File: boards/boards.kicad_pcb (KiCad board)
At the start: 2 copper layers, 34 parts, among them J1 MicroSD, P1 CONN_01X04, P10 , P11 , P12 , P13 CONN_01X02, P2 , P3 , P4 , P5 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

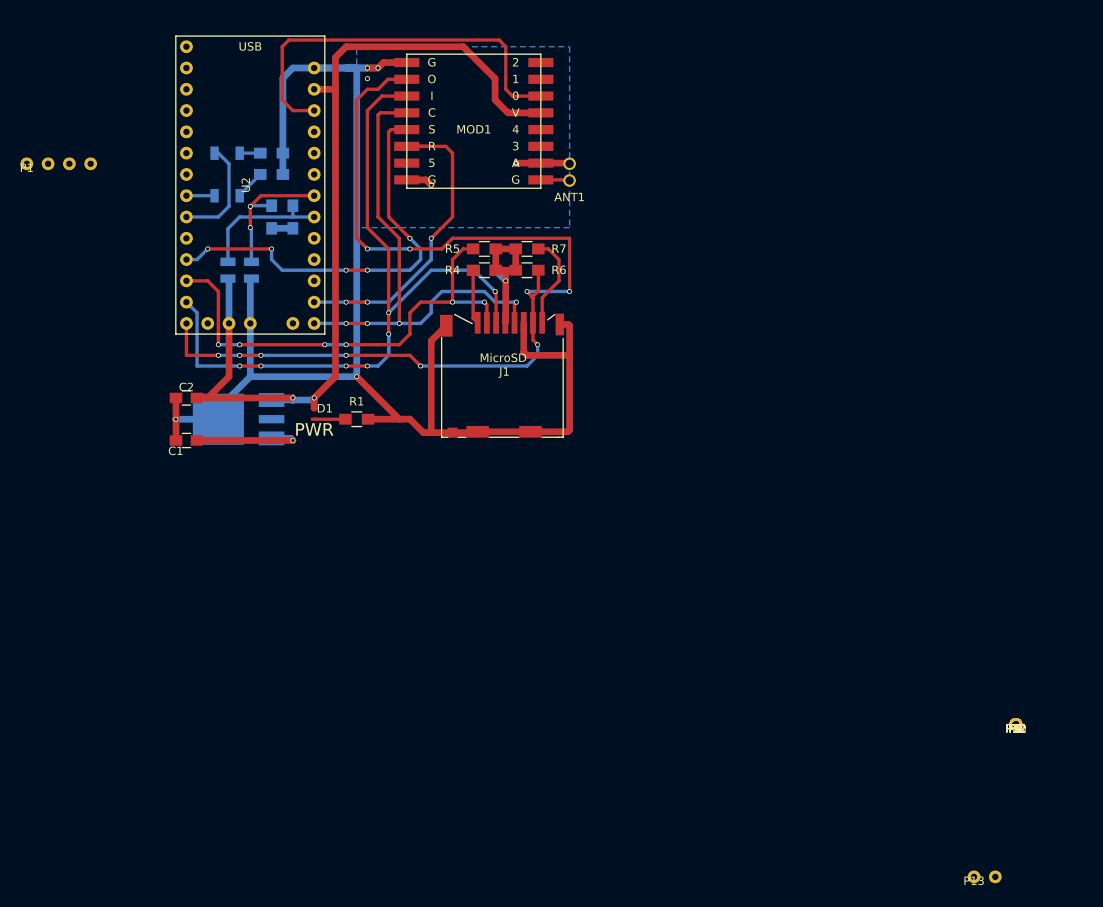
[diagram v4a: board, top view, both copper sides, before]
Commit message: Added power smoothing caps around board.
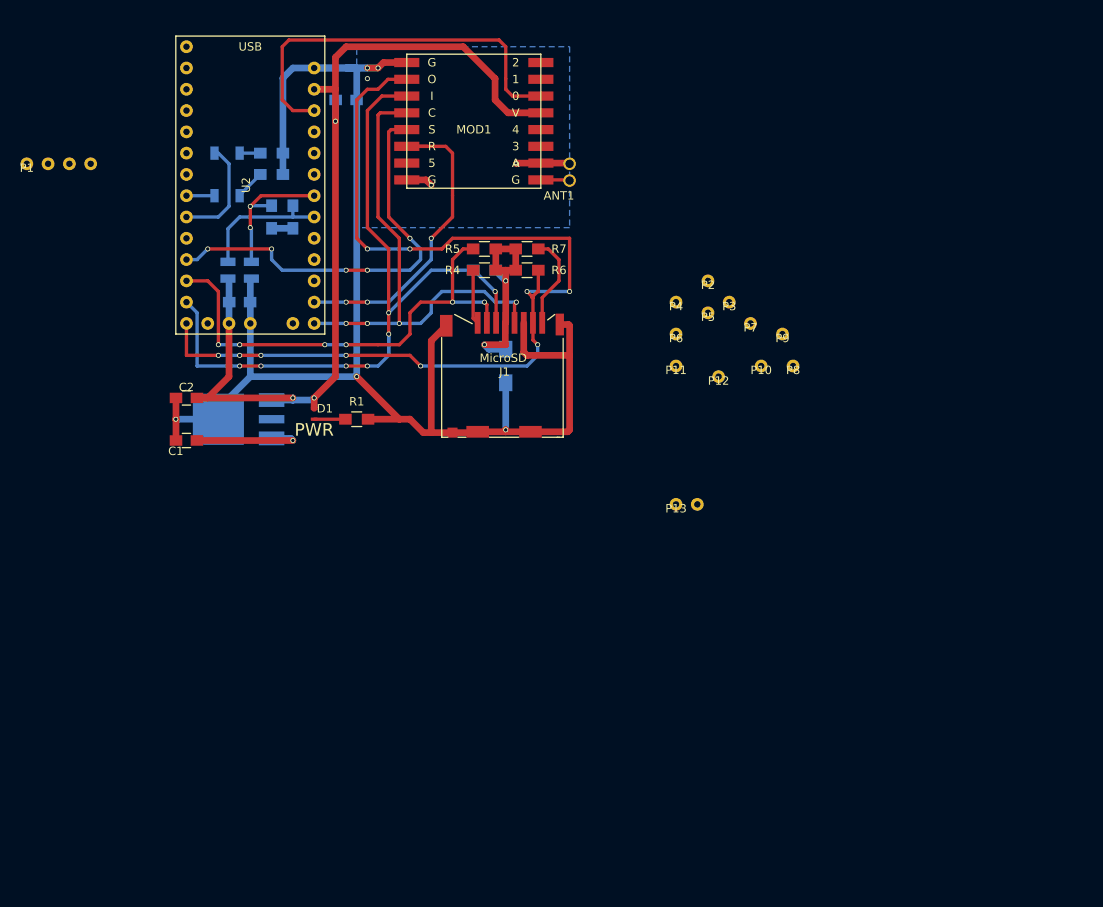
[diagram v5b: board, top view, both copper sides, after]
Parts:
- added C3: 4.7uF, Capacitors_SMD.pretty:C_0805_HandSoldering, B.Cu at (55.9, 54.6)
- added C4: 22uF, Capacitors_SMD.pretty:C_1206_HandSoldering, B.Cu at (87.6, 62.2)
- added C5: 4.7uF, Capacitors_SMD.pretty:C_0805_HandSoldering, B.Cu at (68.6, 30.5)
- moved P4 64.7 mm to (108.0, 54.6)
- moved P2 64.4 mm to (111.8, 52.1)
- moved P6 61.8 mm to (108.0, 58.4)
- moved P5 61.3 mm to (111.8, 55.9)
- moved P3 60.9 mm to (114.3, 54.6)
- moved P11 58.9 mm to (108.0, 62.2)
- moved P7 57.4 mm to (116.8, 57.1)
- moved P13 56.9 mm to (108.0, 78.7)
- moved P12 54.6 mm to (113.0, 63.5)
- moved P9 54.3 mm to (120.7, 58.4)
- moved P10 52.5 mm to (118.1, 62.2)
- moved P8 50.4 mm to (121.9, 62.2)
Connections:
- ANT1 pad 3: Net-(ANT1-Pad1) -> (no net)
- U1 pad 1: +3V3 -> (no net)
- U1 pad 2: GND -> (no net)
- U1 pad 3: VCC -> (no net)
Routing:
- net +3V3: track 129.8 -> 140.3 mm, vias 3 -> 5
- net GND: track 192.1 -> 198.5 mm, vias 6 -> 7

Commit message: Completed design. Not yet checked/verified.
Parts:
- removed P1: CONN_01X04, william-parts:quadruple_pads
- removed P10, P11, P12, P2, P3, P4, P5, P6, P7, P8, P9: , william-parts:single_pad
- removed P13: CONN_01X02, william-parts:double_pads
- added P14: CONN_01X01, william-parts:single_pad, F.Cu at (48.3, 62.2)
- added P15: CONN_01X01, william-parts:single_pad, F.Cu at (74.9, 66.0)
- added P16: CONN_01X01, william-parts:single_pad, F.Cu at (73.7, 63.5)
- added P17: CONN_01X01, william-parts:single_pad, F.Cu at (76.2, 63.5)
- added P18: CONN_01X01, william-parts:single_pad, F.Cu at (74.9, 71.1)
- added P19: CONN_01X01, william-parts:single_pad, F.Cu at (72.4, 71.1)
- added P20: CONN_01X01, william-parts:single_pad, F.Cu at (67.3, 66.0)
- added P21: CONN_01X01, william-parts:single_pad, F.Cu at (69.8, 71.1)
- added P22: CONN_01X01, william-parts:single_pad, F.Cu at (64.8, 71.1)
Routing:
- net +3V3: track 140.3 -> 164.0 mm, vias 5 -> 6
- net GND: track 198.5 -> 219.7 mm
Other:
- board text added: "3V3"
- board text added: "BAT GND"
- board text added: "BAT IN"
- board text added: "GND"
